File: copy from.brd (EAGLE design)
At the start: 31.5 x 30 mm, 16 parts, among them J1 1X2-3.5MM, J2 1X2-3.5MM, J3 1X2-3.5MM

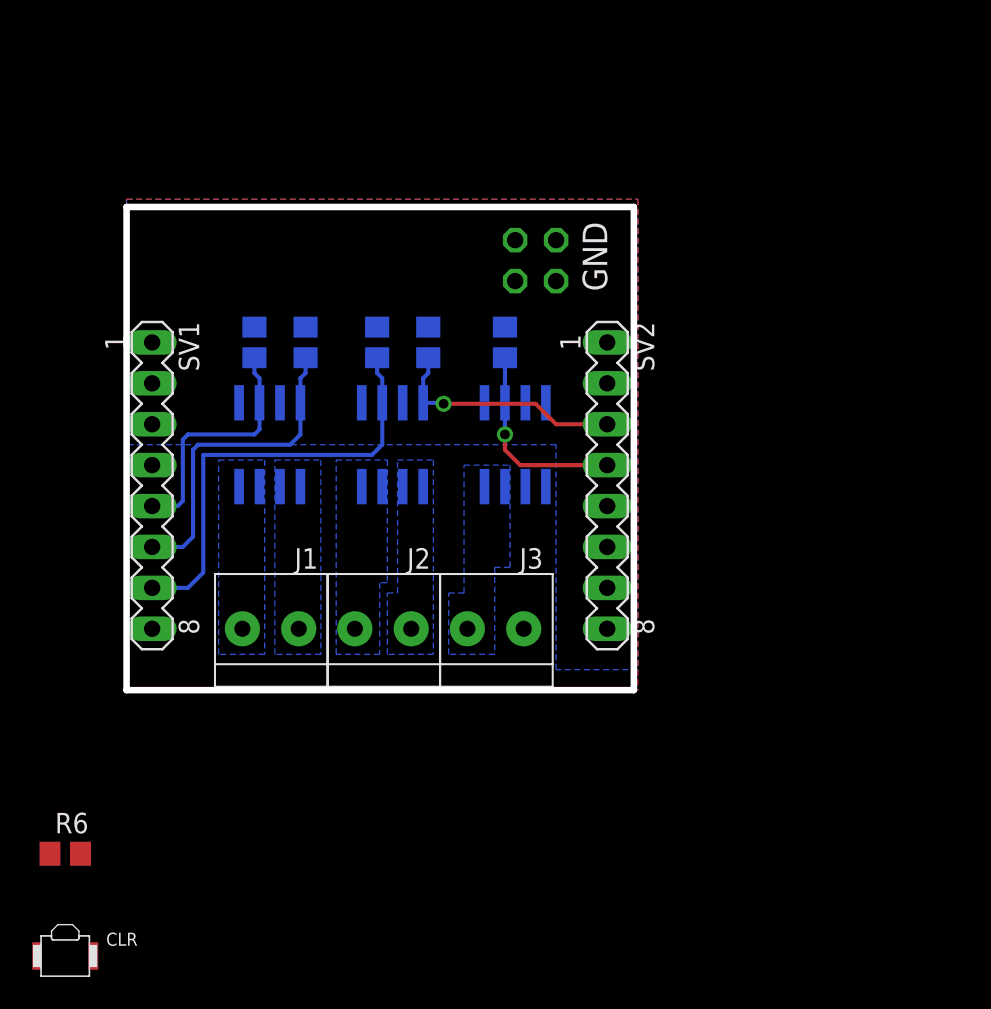
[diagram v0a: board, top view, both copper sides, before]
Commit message: added an ftdi version
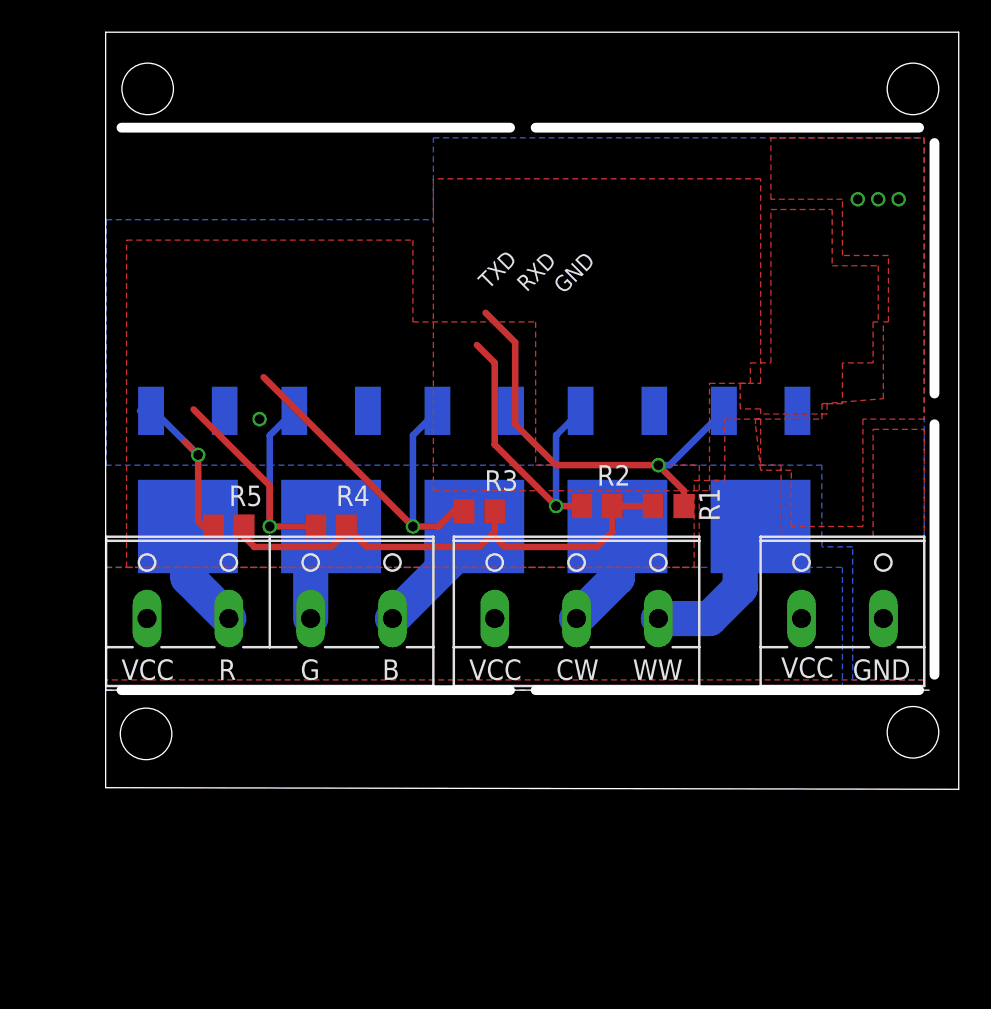
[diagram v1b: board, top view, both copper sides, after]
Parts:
- removed CLR: SPST.B3U-3000P(M), omron:B3U-3000P(M)
- removed J1, J2, J3: 1X2-3.5MM, adafruit:1X2-3.5MM
- removed JP1: (no value), pinhead:2X02
- removed R6: 10k, rcl:R0805
- removed SV1, SV2: (no value), con-lstb:MA08-1
- removed U$1, U$2, U$3: AOD4806, esp12_RGBWW:SO08
- added Q1, Q2, Q3, Q4, Q5: AOD2910SMD, transistor-fet+irf7201:DPAK-3
- added RGB: (no value), con-wago-508:W237-4P
- added VCC: (no value), con-wago-508:W237-132
- added W: (no value), con-wago-508:W237-133
- moved R3 17.5 mm to (21.9, 11.1), flipped to the top, turned to 0 degrees
- moved R5 14.7 mm to (6.35, 10.2), flipped to the top, turned to 0 degrees
- moved R2 14.6 mm to (29.2, 11.4), flipped to the top, turned to 0 degrees
- moved R1 14.4 mm to (33.7, 11.4), flipped to the top, turned to 0 degrees
- moved R4 11.5 mm to (12.7, 10.2), flipped to the top, turned to 0 degrees
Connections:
- removed net ADC: SV1.2
- removed net CH_PD: SV1.3
- removed net GPIO0: SV2.5
- removed net GPIO12: R4.1, SV1.6, U$1.4
- removed net GPIO13: R5.1, SV1.7, U$2.2
- removed net GPIO14: R3.1, SV1.5, U$1.2
- removed net GPIO15: SV2.7
- removed net GPIO16: CLR.2, R6.1, SV1.4
- removed net GPIO2: SV2.6
- removed net GPIO4: R1.2, SV2.4, U$3.2
- removed net GPIO5: R2.1, SV2.3, U$2.4
- removed net REST: SV1.1
- removed net RXD: SV2.2
- removed net TXD: SV2.1
- removed net VCC: CLR.1, SV1.8
- new net RGB-B: Q3.1, R3.1
- new net RGB-CW: Q2.1, R2.1
- new net RGB-G: Q4.1, R4.1
- new net RGB-R: Q5.1, R5.1
- new net RGB-WW: Q1.1, R1.2
- net +12V: now also RGB.1, VCC.1, W.1; no longer J3.1, JP1.1, JP1.3
- net B: now also Q3.4, RGB.4; no longer J1.2, U$1.7, U$1.8
- net CW: now also Q2.4, W.2; no longer J2.1, U$2.5, U$2.6
- net G: now also Q4.4, RGB.3; no longer J1.1, U$1.5, U$1.6
- net GND: now also Q1.3, Q2.3, Q3.3, Q4.3, Q5.3, VCC.2; no longer JP1.2, JP1.4, R6.2, SV2.8, U$1.1, U$1.3, U$2.1, U$2.3, U$3.1
- net R: now also Q5.4, RGB.2; no longer J2.2, U$2.7, U$2.8
- net WW: now also Q1.4, W.3; no longer J3.2, U$3.7, U$3.8
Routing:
- net GND: track 0.00 -> 32.0 mm, vias 0 -> 4
- net GPIO13: track 27.8 -> 0.00 mm
- net RGB-WW: track 0.00 -> 26.3 mm, vias 0 -> 1
- net RGB-B: track 0.00 -> 24.5 mm, vias 0 -> 1
- net RGB-CW: track 0.00 -> 20.2 mm, vias 0 -> 1
- net GPIO12: track 20.2 -> 0.00 mm
- net RGB-G: track 0.00 -> 19.9 mm, vias 0 -> 1
- net GPIO14: track 15.5 -> 0.00 mm
- net GPIO5: track 14.9 -> 0.00 mm, vias 1 -> 0
- net GPIO4: track 12.5 -> 0.00 mm, vias 1 -> 0
- net RGB-R: track 0.00 -> 11.1 mm, vias 0 -> 1
- net WW: track 0.00 -> 10.2 mm
- net B: track 0.00 -> 7.18 mm
- net R: track 0.00 -> 6.77 mm
- net CW: track 0.00 -> 6.77 mm
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- added copper zone on layer 16, net +12V
- added copper zone on layer 1, net +3V3
- added copper zone on layer 1, net GND
- added copper zone on layer 1, net PH
- removed copper zone on layer 16, net B
- removed copper zone on layer 16, net CW
- removed copper zone on layer 16, net G
- removed copper zone on layer 16, net R
- removed copper zone on layer 16, net WW
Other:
- board size 31.5 x 30 mm -> 53 x 47 mm
- board text added: "B"
- board text added: "CW"
- board text added: "G"
- board text added: "R"
- board text added: "RXD"
- board text added: "TXD"
- board text added: "VCC"
- board text added: "WW"
